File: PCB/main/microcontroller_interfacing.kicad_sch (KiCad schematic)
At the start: 14 parts, among them J5 USB_B_Micro, SW1 C13828, SW2 C13828

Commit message: updated gerbers and finalized PCB
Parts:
- C4: value CT41G-0402-2X1-16V-0.1μF-K(N) -> 0.1μF; LCSC (none) -> C141382; Populate (none) -> P; Price (none) -> 0.0032
- D4: LCSC (none) -> C2480; Populate (none) -> P; Price (none) -> 0.0179; Spice_Netlist_Enabled Y -> (none)
- EEPROM1: LCSC (none) -> C6482; Populate (none) -> P; Price (none) -> 1.4287
- FTDI(UART)1: LCSC (none) -> C84681; Populate (none) -> P; Price (none) -> 0.5589; Spice_Netlist_Enabled (none) -> Center; Spice_Primitive (none) -> Center
- J5: LCSC (none) -> C404969; Populate (none) -> P; Price (none) -> 0.047
- R14: LCSC (none) -> C25804; Populate (none) -> P; Price (none) -> 0.0012
- R15, R16, R17: LCSC (none) -> C21190; Populate (none) -> P; Price (none) -> 0.0012
- R18: LCSC (none) -> C23162; Populate (none) -> P; Price (none) -> 0.0012
- R19, R20: LCSC (none) -> C21189; Populate (none) -> P; Price (none) -> 0.0012
- SW1, SW2: LCSC (none) -> C13828; Populate (none) -> P; Price (none) -> 0.0394
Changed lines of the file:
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@@
       (effects (font (size 1.27 1.27)) hide)
     )
-    (property "Datasheet" "~" (id 3) (at 273.558 38.354 0)
+    (property "Datasheet" "https://datasheet.lcsc.com/szlcsc/1912111437_Dongguan-Guangzhu-Industrial-C13828_C13828.pdf" (id 3) (at 273.558 38.354 0)
+      (effects (font (size 1.27 1.27)) hide)
+    )
+    (property "LCSC" "C13828" (id 4) (at 268.478 38.354 0)
+      (effects (font (size 1.27 1.27)) hide)
+    )
+    (property "Populate" "P" (id 5) (at 268.478 38.354 0)
+      (effects (font (size 1.27 1.27)) hide)
+    )
+    (property "Price" "0.0394" (id 6) (at 268.478 38.354 0)
       (effects (font (size 1.27 1.27)) hide)
     )
@@
       (effects (font (size 1.27 1.27)) hide)
     )
-    (property "Datasheet" "~" (id 3) (at 255.27 84.074 0)
+    (property "Datasheet" "https://datasheet.lcsc.com/lcsc/2110252030_UNI-ROYAL-Uniroyal-Elec-0603WAF1001T5E_C21190.pdf" (id 3) (at 255.27 84.074 0)
+      (effects (font (size 1.27 1.27)) hide)
+    )
+    (property "LCSC" "C21190" (id 4) (at 255.27 84.074 0)
+      (effects (font (size 1.27 1.27)) hide)
+    )
+    (property "Populate" "P" (id 5) (at 255.27 84.074 0)
+      (effects (font (size 1.27 1.27)) hide)
+    )
+    (property "Price" "0.0012" (id 6) (at 255.27 84.074 0)
       (effects (font (size 1.27 1.27)) hide)
     )
@@
       (effects (font (size 1.27 1.27)) hide)
     )
-    (property "Datasheet" "~" (id 3) (at 255.27 107.442 0)
+    (property "Datasheet" "https://datasheet.lcsc.com/lcsc/2110252030_UNI-ROYAL-Uniroyal-Elec-0603WAF1001T5E_C21190.pdf" (id 3) (at 255.27 107.442 0)
+      (effects (font (size 1.27 1.27)) hide)
+    )
+    (property "LCSC" "C21190" (id 4) (at 255.27 107.442 0)
+      (effects (font (size 1.27 1.27)) hide)
+    )
+    (property "Populate" "P" (id 5) (at 255.27 107.442 0)
+      (effects (font (size 1.27 1.27)) hide)
+    )
+    (property "Price" "0.0012" (id 6) (at 255.27 107.442 0)
       (effects (font (size 1.27 1.27)) hide)
     )
@@
     )
     (property "Datasheet" "https://www.onsemi.cn/PowerSolutions/document/CAT24C256-D.PDF" (id 3) (at 206.756 143.256 0)
+      (effects (font (size 1.27 1.27)) hide)
+    )
+    (property "LCSC" "C6482" (id 4) (at 206.756 143.256 0)
+      (effects (font (size 1.27 1.27)) hide)
+    )
+    (property "Populate" "P" (id 5) (at 206.756 143.256 0)
+      (effects (font (size 1.27 1.27)) hide)
+    )
+    (property "Price" "1.4287" (id 6) (at 206.756 143.256 0)
       (effects (font (size 1.27 1.27)) hide)
     )
@@
       (effects (font (size 1.27 1.27)) hide)
     )
-    (property "Datasheet" "~" (id 3) (at 268.478 51.562 0)
+    (property "Datasheet" "https://datasheet.lcsc.com/lcsc/2110252130_UNI-ROYAL-Uniroyal-Elec-0603WAF4701T5E_C23162.pdf" (id 3) (at 268.478 51.562 0)
+      (effects (font (size 1.27 1.27)) hide)
+    )
+    (property "LCSC" "C23162" (id 4) (at 268.478 51.562 0)
+      (effects (font (size 1.27 1.27)) hide)
+    )
+    (property "Populate" "P" (id 5) (at 268.478 51.562 0)
+      (effects (font (size 1.27 1.27)) hide)
+    )
+    (property "Price" "0.0012" (id 6) (at 268.478 51.562 0)
       (effects (font (size 1.27 1.27)) hide)
     )
@@
       (effects (font (size 1.27 1.27)) hide)
     )
-    (property "Datasheet" "~" (id 3) (at 231.14 24.384 0)
+    (property "Datasheet" "https://datasheet.lcsc.com/lcsc/2110252030_UNI-ROYAL-Uniroyal-Elec-0603WAF0000T5E_C21189.pdf" (id 3) (at 231.14 24.384 0)
+      (effects (font (size 1.27 1.27)) hide)
+    )
+    (property "LCSC" "C21189" (id 4) (at 231.14 24.384 0)
+      (effects (font (size 1.27 1.27)) hide)
+    )
+    (property "Populate" "P" (id 5) (at 231.14 24.384 0)
+      (effects (font (size 1.27 1.27)) hide)
+    )
+    (property "Price" "0.0012" (id 6) (at 231.14 24.384 0)
       (effects (font (size 1.27 1.27)) hide)
     )
@@
     )
     (property "Datasheet" "https://datasheet.lcsc.com/szlcsc/Jiangsu-Qin-Heng-CH340C_C84681.pdf" (id 3) (at 201.422 18.796 0)
+      (effects (font (size 1.27 1.27)) hide)
+    )
+    (property "LCSC" "C84681" (id 4) (at 210.312 39.116 0)
+      (effects (font (size 1.27 1.27)) hide)
+    )
+    (property "Populate" "P" (id 5) (at 210.312 39.116 0)
+      (effects (font (size 1.27 1.27)) hide)
+    )
+    (property "Price" "0.5589" (id 6) (at 210.312 39.116 0)
+      (effects (font (size 1.27 1.27)) hide)
+    )
+    (property "Spice_Netlist_Enabled" "Center" (id 7) (at 210.312 39.116 0)
+      (effects (font (size 1.27 1.27)) hide)
+    )
+    (property "Spice_Primitive" "Center" (id 8) (at 210.312 39.116 0)
       (effects (font (size 1.27 1.27)) hide)
     )
@@
       (effects (font (size 1.27 1.27)) hide)
     )
-    (property "Datasheet" "~" (id 3) (at 255.27 99.822 0)
+    (property "Datasheet" "https://datasheet.lcsc.com/lcsc/2110252030_UNI-ROYAL-Uniroyal-Elec-0603WAF1001T5E_C21190.pdf" (id 3) (at 255.27 99.822 0)
+      (effects (font (size 1.27 1.27)) hide)
+    )
+    (property "LCSC" "C21190" (id 4) (at 255.27 99.822 0)
+      (effects (font (size 1.27 1.27)) hide)
+    )
+    (property "Populate" "P" (id 5) (at 255.27 99.822 0)
+      (effects (font (size 1.27 1.27)) hide)
+    )
+    (property "Price" "0.0012" (id 6) (at 255.27 99.822 0)
       (effects (font (size 1.27 1.27)) hide)
     )
@@
       (effects (font (size 1.27 1.27)) hide)
     )
-    (property "Datasheet" "~" (id 3) (at 255.016 150.876 0)
+    (property "Datasheet" "https://datasheet.lcsc.com/lcsc/2110260030_UNI-ROYAL-Uniroyal-Elec-0603WAF1002T5E_C25804.pdf" (id 3) (at 255.016 150.876 0)
+      (effects (font (size 1.27 1.27)) hide)
+    )
+    (property "LCSC" "C25804" (id 4) (at 255.016 150.876 0)
+      (effects (font (size 1.27 1.27)) hide)
+    )
+    (property "Populate" "P" (id 5) (at 255.016 150.876 0)
+      (effects (font (size 1.27 1.27)) hide)
+    )
+    (property "Price" "0.0012" (id 6) (at 255.016 150.876 0)
       (effects (font (size 1.27 1.27)) hide)
     )
@@
       (effects (font (size 1.27 1.27)) hide)
     )
-    (property "Datasheet" "~" (id 3) (at 231.14 38.1 0)
+    (property "Datasheet" "https://datasheet.lcsc.com/lcsc/2110252030_UNI-ROYAL-Uniroyal-Elec-0603WAF0000T5E_C21189.pdf" (id 3) (at 231.14 38.1 0)
+      (effects (font (size 1.27 1.27)) hide)
+    )
+    (property "LCSC" "C21189" (id 4) (at 231.14 38.1 0)
+      (effects (font (size 1.27 1.27)) hide)
+    )
+    (property "Populate" "P" (id 5) (at 231.14 38.1 0)
+      (effects (font (size 1.27 1.27)) hide)
+    )
+    (property "Price" "0.0012" (id 6) (at 231.14 38.1 0)
       (effects (font (size 1.27 1.27)) hide)
     )
@@
       (effects (font (size 1.27 1.27)) hide)
     )
-    (property "Datasheet" "~" (id 3) (at 240.03 90.424 0)
-      (effects (font (size 1.27 1.27)) hide)
-    )
-    (property "Spice_Netlist_Enabled" "Y" (id 4) (at 240.03 90.424 0)
+    (property "Datasheet" "https://datasheet.lcsc.com/lcsc/2105061432_MDD-Microdiode-Electronics--SS14_C2480.pdf" (id 3) (at 240.03 90.424 0)
+      (effects (font (size 1.27 1.27)) hide)
+    )
+    (property "Spice_Netlist_Enabled" "" (id 4) (at 240.03 90.424 0)
       (effects (font (size 1.27 1.27)) (justify left) hide)
     )
@@
       (effects (font (size 1.27 1.27)) (justify left) hide)
     )
+    (property "LCSC" "C2480" (id 6) (at 240.03 90.424 0)
+      (effects (font (size 1.27 1.27)) hide)
+    )
+    (property "Populate" "P" (id 7) (at 240.03 90.424 0)
+      (effects (font (size 1.27 1.27)) hide)
+    )
+    (property "Price" "0.0179" (id 8) (at 240.03 90.424 0)
+      (effects (font (size 1.27 1.27)) hide)
+    )
     (pin "1")
     (pin "2")
@@
     (in_bom yes) (on_board yes)
     (property "Reference" "C4" (id 0) (at 205.232 13.716 90))
-    (property "Value" "CT41G-0402-2X1-16V-0.1μF-K(N)" (id 1) (at 205.232 15.748 90))
+    (property "Value" "0.1μF" (id 1) (at 205.232 15.748 90))
     (property "Footprint" "Capacitor_SMD:C_0201_0603Metric" (id 2) (at 205.232 18.288 0)
       (effects (font (size 1.27 1.27)) hide)
     )
-    (property "Datasheet" "~" (id 3) (at 205.232 18.288 0)
+    (property "Datasheet" "https://datasheet.lcsc.com/lcsc/1809291616_TORCH-CT41-0603-2X1-25V-0-1-F-K-N_C139738.pdf" (id 3) (at 205.232 18.288 0)
+      (effects (font (size 1.27 1.27)) hide)
+    )
+    (property "LCSC" "C141382" (id 4) (at 205.232 18.288 0)
+      (effects (font (size 1.27 1.27)) hide)
+    )
+    (property "Populate" "P" (id 5) (at 205.232 18.288 0)
+      (effects (font (size 1.27 1.27)) hide)
+    )
+    (property "Price" "0.0032" (id 6) (at 205.232 18.288 0)
       (effects (font (size 1.27 1.27)) hide)
     )
@@
     )
     (property "Datasheet" "~" (id 3) (at 211.074 96.774 0)
+      (effects (font (size 1.27 1.27)) hide)
+    )
+    (property "LCSC" "C404969" (id 4) (at 207.264 95.504 0)
+      (effects (font (size 1.27 1.27)) hide)
+    )
+    (property "Populate" "P" (id 5) (at 207.264 95.504 0)
+      (effects (font (size 1.27 1.27)) hide)
+    )
+    (property "Price" "0.047" (id 6) (at 207.264 95.504 0)
       (effects (font (size 1.27 1.27)) hide)
     )
@@
       (effects (font (size 1.27 1.27)) hide)
     )
-    (property "Datasheet" "~" (id 3) (at 260.096 138.176 0)
-      (effects (font (size 1.27 1.27)) hide)
-    )
+    (property "Datasheet" "https://datasheet.lcsc.com/szlcsc/1912111437_Dongguan-Guangzhu-Industrial-C13828_C13828.pdf" (id 3) (at 260.096 138.176 0)
+      (effects (font (size 1.27 1.27)) hide)
+    )
+    (property "LCSC" "C13828" (id 4) (at 255.016 138.176 0)
+      (effects (font (size 1.27 1.27)) hide)
+    )
+    (property "Populate" "P" (id 5) (at 255.016 138.176 0)
+      (effects (font (size 1.27 1.27)) hide)
+    )
+    (property "Price" "0.0394" (id 6) (at 255.016 138.176 0)
+      (effects (font (size 1.27 1.27)) hide)
+    )

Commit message: updated PCB & Assembly file
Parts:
- FTDI1: renamed from FTDI(UART)1; footprint CH340C:SOIC127P600X180-16N -> Package_SO:SOP-16_3.9x9.9mm_P1.27mm
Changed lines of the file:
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@@
   (symbol (lib_id "Interface_USB:CH340C") (at 210.312 39.116 0) (unit 1)
     (in_bom yes) (on_board yes) (fields_autoplaced)
-    (property "Reference" "FTDI(UART)1" (id 0) (at 212.3314 54.61 0)
+    (property "Reference" "FTDI1" (id 0) (at 212.3314 54.61 0)
       (effects (font (size 1.27 1.27)) (justify left))
     )
@@
       (effects (font (size 1.27 1.27)) (justify left))
     )
-    (property "Footprint" "CH340C:SOIC127P600X180-16N" (id 2) (at 211.582 53.086 0)
+    (property "Footprint" "Package_SO:SOP-16_3.9x9.9mm_P1.27mm" (id 2) (at 211.582 53.086 0)
       (effects (font (size 1.27 1.27)) (justify left) hide)
     )

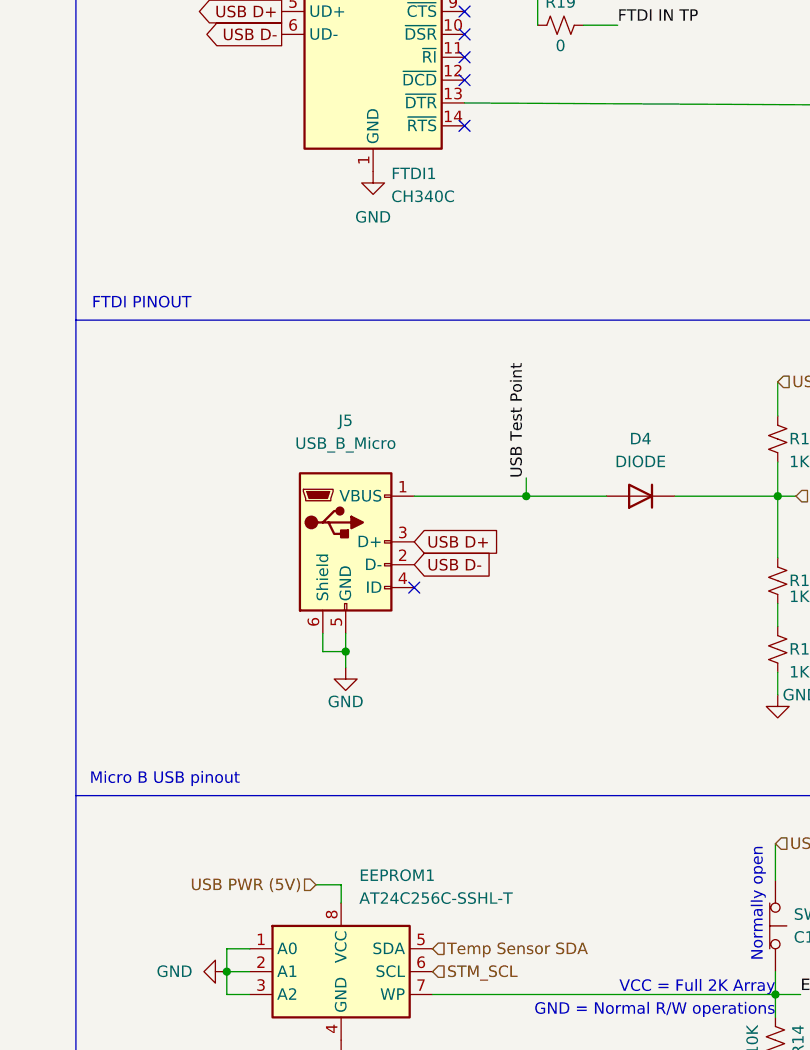
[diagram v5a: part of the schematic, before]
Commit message: rewired PCB and changed relevant footprints. production files regenerated
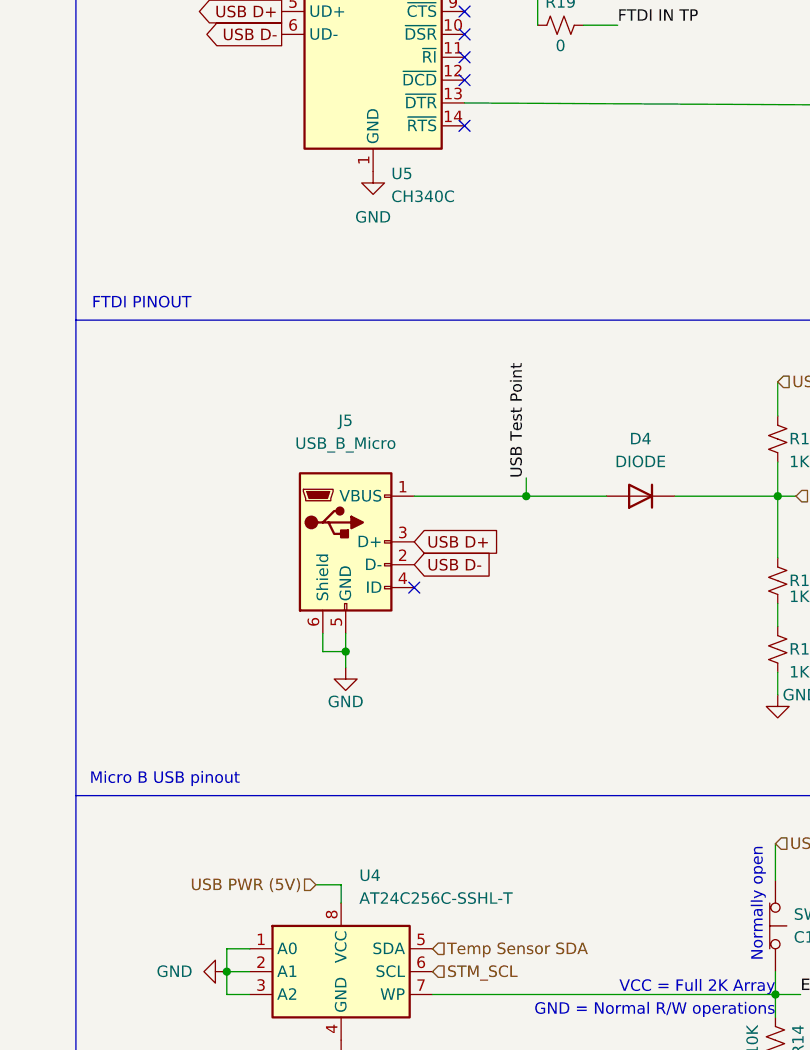
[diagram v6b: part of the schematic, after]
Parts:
- R14, R15, R16, R17, R18, R19, R20: footprint Resistor_SMD:R_0201_0603Metric -> Resistor_SMD:R_0603_1608Metric
- renumbered EEPROM1 to U4, FTDI1 to U5
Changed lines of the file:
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@@
       (effects (font (size 1.27 1.27)) (justify left))
     )
-    (property "Footprint" "Resistor_SMD:R_0201_0603Metric" (id 2) (at 255.27 84.074 0)
+    (property "Footprint" "Resistor_SMD:R_0603_1608Metric" (id 2) (at 255.27 84.074 0)
       (effects (font (size 1.27 1.27)) hide)
     )
@@
       (effects (font (size 1.27 1.27)) (justify left))
     )
-    (property "Footprint" "Resistor_SMD:R_0201_0603Metric" (id 2) (at 255.27 107.442 0)
+    (property "Footprint" "Resistor_SMD:R_0603_1608Metric" (id 2) (at 255.27 107.442 0)
       (effects (font (size 1.27 1.27)) hide)
     )
@@
   (symbol (lib_id "Memory_EEPROM:CAT24C256") (at 206.756 143.256 0) (unit 1)
     (in_bom yes) (on_board yes) (fields_autoplaced)
-    (property "Reference" "EEPROM1" (id 0) (at 208.7754 132.588 0)
+    (property "Reference" "U4" (id 0) (at 208.7754 132.588 0)
       (effects (font (size 1.27 1.27)) (justify left))
     )
@@
     (property "Reference" "R18" (id 0) (at 271.018 51.562 90))
     (property "Value" "4K7" (id 1) (at 265.938 51.562 90))
-    (property "Footprint" "Resistor_SMD:R_0201_0603Metric" (id 2) (at 268.478 51.562 0)
+    (property "Footprint" "Resistor_SMD:R_0603_1608Metric" (id 2) (at 268.478 51.562 0)
       (effects (font (size 1.27 1.27)) hide)
     )
@@
     (property "Reference" "R20" (id 0) (at 231.14 22.352 90))
     (property "Value" "0" (id 1) (at 231.14 26.416 90))
-    (property "Footprint" "Resistor_SMD:R_0201_0603Metric" (id 2) (at 231.14 24.384 0)
+    (property "Footprint" "Resistor_SMD:R_0603_1608Metric" (id 2) (at 231.14 24.384 0)
       (effects (font (size 1.27 1.27)) hide)
     )
@@
   (symbol (lib_id "Interface_USB:CH340C") (at 210.312 39.116 0) (unit 1)
     (in_bom yes) (on_board yes) (fields_autoplaced)
-    (property "Reference" "FTDI1" (id 0) (at 212.3314 54.61 0)
+    (property "Reference" "U5" (id 0) (at 212.3314 54.61 0)
       (effects (font (size 1.27 1.27)) (justify left))
     )
@@
       (effects (font (size 1.27 1.27)) (justify left))
     )
-    (property "Footprint" "Resistor_SMD:R_0201_0603Metric" (id 2) (at 255.27 99.822 0)
+    (property "Footprint" "Resistor_SMD:R_0603_1608Metric" (id 2) (at 255.27 99.822 0)
       (effects (font (size 1.27 1.27)) hide)
     )
@@
     (property "Reference" "R14" (id 0) (at 257.556 150.876 90))
     (property "Value" "10K" (id 1) (at 252.476 150.876 90))
-    (property "Footprint" "Resistor_SMD:R_0201_0603Metric" (id 2) (at 255.016 150.876 0)
+    (property "Footprint" "Resistor_SMD:R_0603_1608Metric" (id 2) (at 255.016 150.876 0)
       (effects (font (size 1.27 1.27)) hide)
     )
@@
     (property "Reference" "R19" (id 0) (at 231.14 35.56 90))
     (property "Value" "0" (id 1) (at 231.14 40.386 90))
-    (property "Footprint" "Resistor_SMD:R_0201_0603Metric" (id 2) (at 231.14 38.1 0)
-      (effects (font (size 1.27 1.27)) hide)
-    )
+    (property "Footprint" "Resistor_SMD:R_0603_1608Metric" (id 2) (at 231.14 38.1 0)
+      (effects (font (size 1.27 1.27)) hide)
+    )
